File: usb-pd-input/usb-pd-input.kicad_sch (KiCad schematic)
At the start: 2 parts, among them J1 USB_C_Receptacle, U1 CH224K

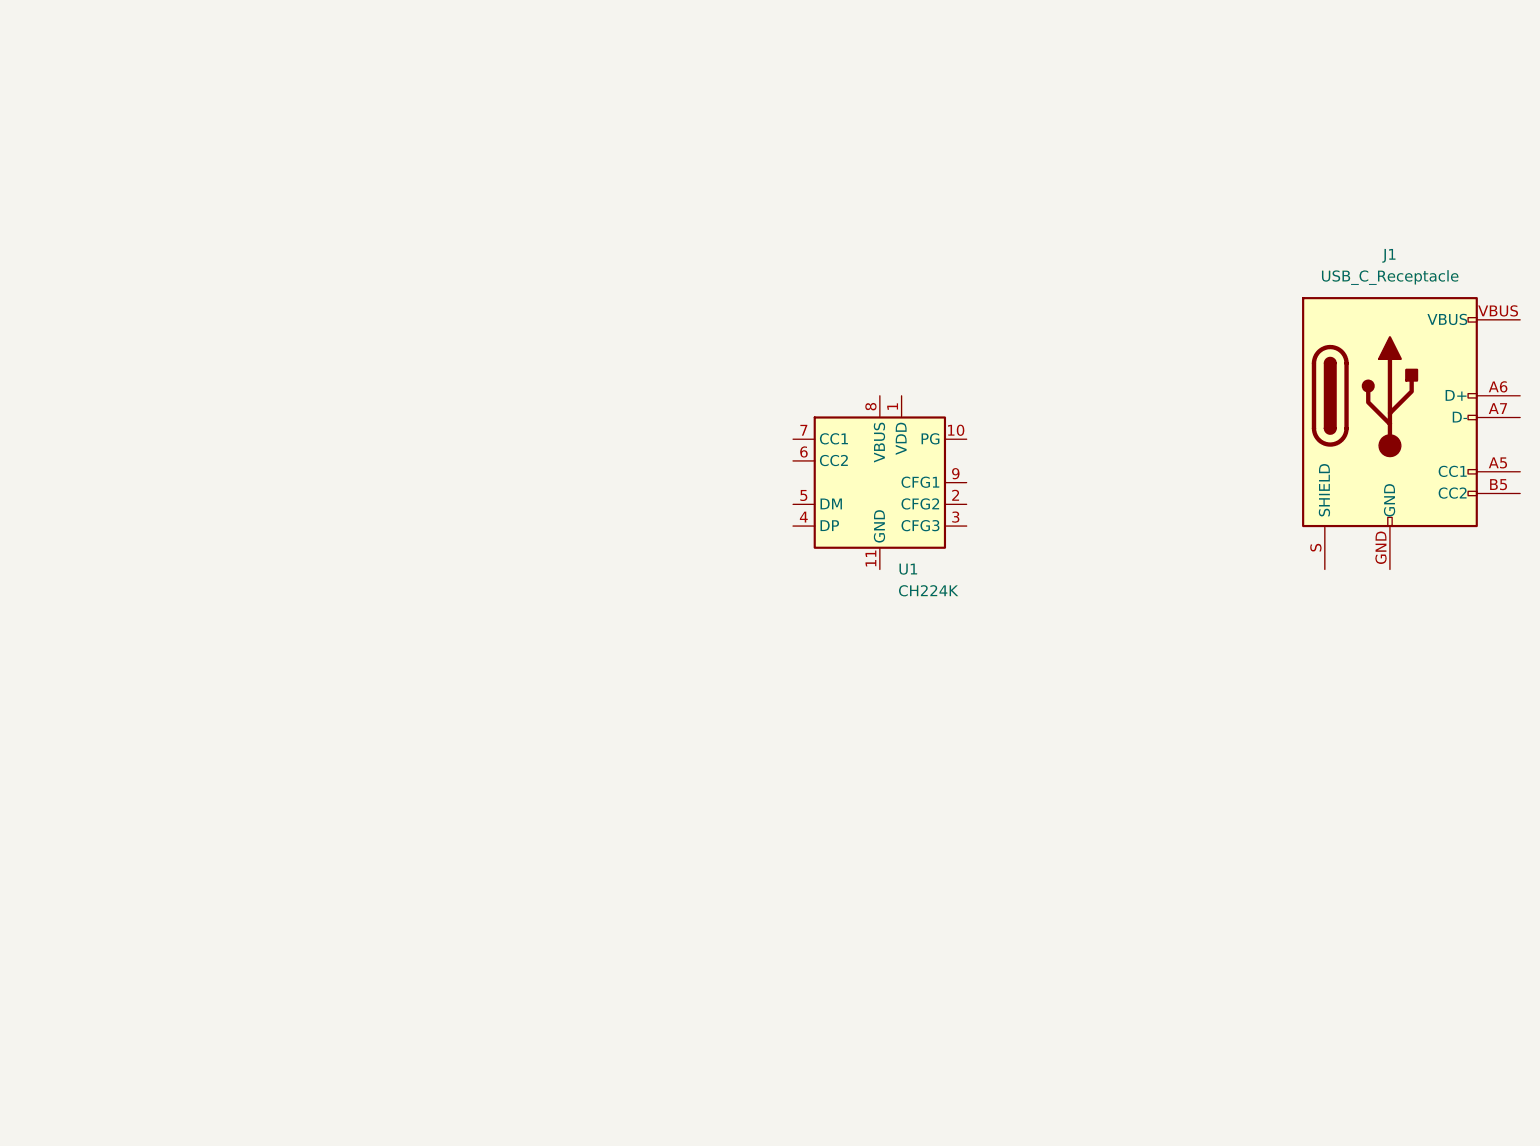
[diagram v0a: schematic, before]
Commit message: Added USB-PD rough-in
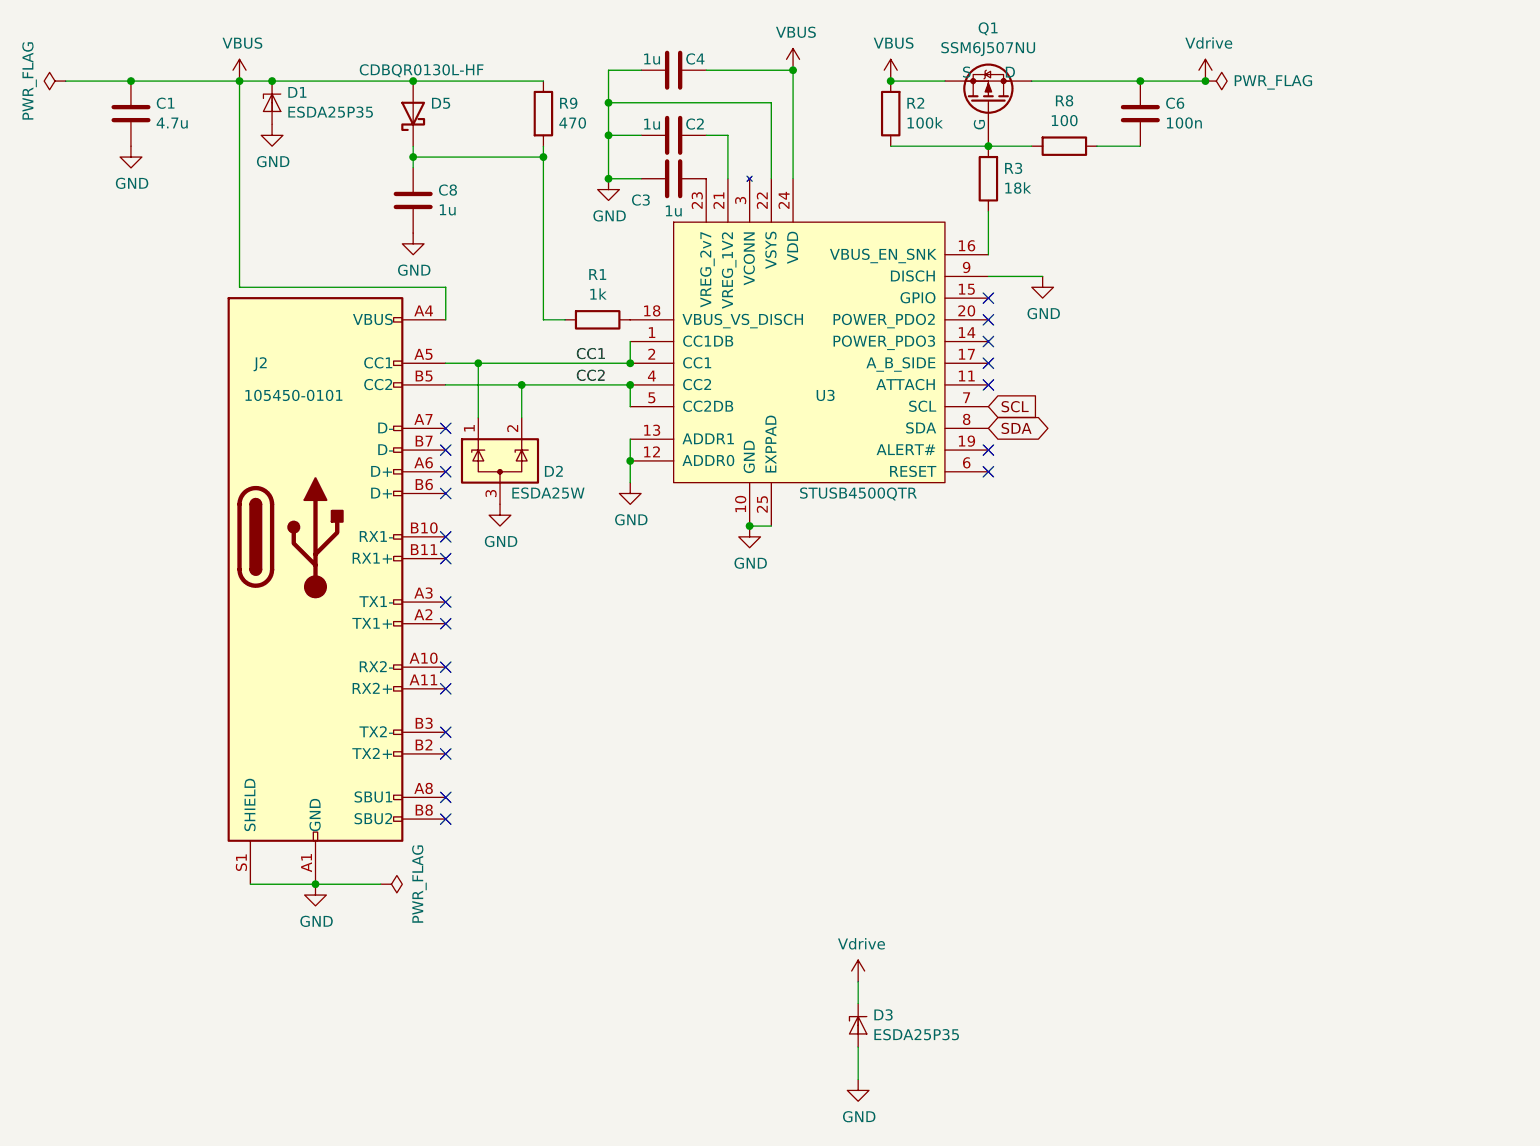
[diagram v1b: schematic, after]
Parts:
- removed J1: USB_C_Receptacle, PCM_SparkFun-Connector:USB-C_16, symbol PCM_SparkFun-Connector:USB_C_Receptacle
- removed U1: CH224K, Package_SO:SSOP-10-1EP_3.9x4.9mm_P1mm_EP2.1x3.3mm, symbol Interface_USB:CH224K
- added C1: 4.7u, Capacitor_SMD:C_0603_1608Metric, symbol Device:C
- added C2, C3, C4: 1u, Capacitor_SMD:C_0603_1608Metric, symbol Device:C
- added C6: 100n, Capacitor_SMD:C_0402_1005Metric, symbol Device:C
- added C8: 1u, Capacitor_SMD:C_0402_1005Metric, symbol Device:C
- added D1, D3: ESDA25P35, rhinocerose-diodes:ESDA25P351U1M, symbol symbol:ESDA25P35
- added D2: ESDA25W, Package_TO_SOT_SMD:SOT-323_SC-70, symbol symbol:ESDA25W
- added D5: D_Schottky, Diode_SMD:D_0402_1005Metric, symbol Device:D_Schottky
- added J2: 105450-0101, fpx:MOLEX_105450-0101, symbol fpx-rescue:USB_C_Receptacle-Connector
- added Q1: SSM6J507NU, rhinocerose-transistors:SSM6J507NULF, symbol symbol:SSM6J507NU
- added R1: 1k, Resistor_SMD:R_0402_1005Metric, symbol Device:R
- added R2: 100k, Resistor_SMD:R_0402_1005Metric, symbol Device:R
- added R3: 18k, Resistor_SMD:R_0402_1005Metric, symbol Device:R
- added R8: 100, Resistor_SMD:R_0402_1005Metric, symbol Device:R
- added R9: 470, Resistor_SMD:R_0402_1005Metric, symbol Device:R
- added U3: STUSB4500, Package_DFN_QFN:QFN-24-1EP_4x4mm_P0.5mm_EP2.7x2.6mm, symbol symbol:STUSB4500
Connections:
- new net: Q1.3 (G), R2.1, R3.2, R8.2
- new net: C3.1, U3.23 (VREG_2v7)
- new net: C2.1, U3.21 (VREG_1V2)
- new net: R1.1, U3.18 (VBUS_VS_DISCH)
- new net: C8.1, D5.1 (K), R1.2, R9.2
- new net: R3.1, U3.16 (VBUS_EN_SNK)
- new net: C6.2, R8.1
- new net CC1: D2.1 (K), J2.A5 (CC1), U3.1 (CC1DB), U3.2 (CC1)
- new net CC2: D2.2 (K), J2.B5 (CC2), U3.4 (CC2), U3.5 (CC2DB)
- new net GND: C1.2, C2.2, C3.2, C4.2, C8.2, D1.2 (A), D2.3 (A), D3.2 (A), J2.A1 (GND), J2.A12 (GND), J2.B1 (GND), J2.B12 (GND), J2.S1 (SHIELD), U3.10 (GND), U3.12 (ADDR0), U3.13 (ADDR1), U3.22 (VSYS), U3.25 (EXPPAD), U3.9 (DISCH)
- new net SCL: U3.7 (SCL)
- new net SDA: U3.8 (SDA)
- new net VBUS: C1.1, C4.1, D1.1 (K1), D5.2 (A), J2.A4 (VBUS), J2.A9 (VBUS), J2.B4 (VBUS), J2.B9 (VBUS), Q1.4 (S), Q1.S, R2.2, R9.1, U3.24 (VDD)
- new net Vdrive: C6.1, D3.1 (K1), Q1.1 (D), Q1.2 (D), Q1.5 (D), Q1.6 (D), Q1.D
- no-connect marks 0 -> 21

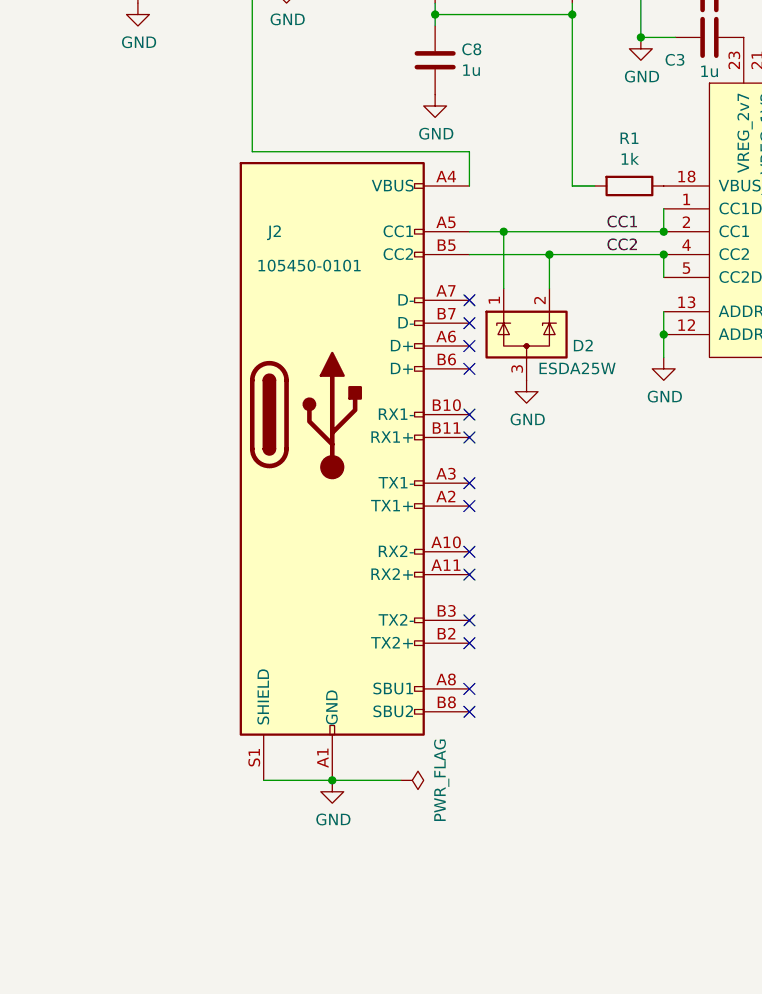
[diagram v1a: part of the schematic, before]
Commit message: Added CH224 schematic
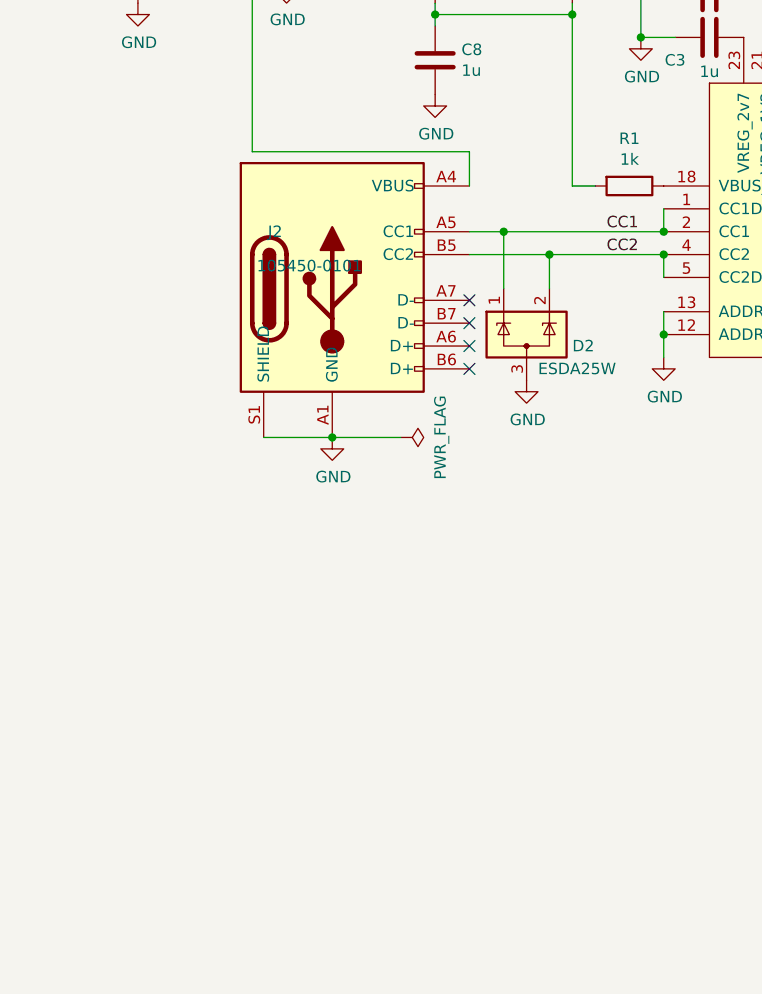
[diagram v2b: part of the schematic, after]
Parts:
- J2: footprint fpx:MOLEX_105450-0101 -> rhinocerose-jacks:CUI_UJ20-C-V-C-2-SMT-TR; symbol fpx-rescue:USB_C_Receptacle-Connector -> rhinocerose-connectors:UJ20-C-V-C-2-SMT-TR; CREATOR (none) -> KARTHIK; MANUFACTURER (none) -> Same Sky; MAXIMUM_PACKAGE_HEIGHT (none) -> 10.75 mm; PARTREV (none) -> 1.02; STANDARD (none) -> Manufacturer Recommendation
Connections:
- no-connect marks 21 -> 11
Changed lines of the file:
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@@
 	)
 	(junction
-		(at 57.15 127)
+		(at 57.15 88.9)
 		(diameter 0)
 		(color 0 0 0 0)
@@
 	)
 	(no_connect
-		(at 72.39 93.98)
-	)
-	(no_connect
 		(at 72.39 78.74)
 	)
 	(no_connect
-		(at 72.39 111.76)
-	)
-	(no_connect
-		(at 72.39 109.22)
-	)
-	(no_connect
-		(at 72.39 104.14)
-	)
-	(no_connect
 		(at 72.39 73.66)
 	)
@@
 	)
 	(no_connect
-		(at 72.39 96.52)
-	)
-	(no_connect
-		(at 72.39 119.38)
-	)
-	(no_connect
 		(at 135.89 78.74)
 	)
@@
 	)
 	(no_connect
-		(at 72.39 88.9)
-	)
-	(no_connect
-		(at 72.39 116.84)
-	)
-	(no_connect
 		(at 135.89 66.04)
 	)
@@
 		(at 135.89 63.5)
 	)
-	(no_connect
-		(at 72.39 86.36)
-	)
-	(no_connect
-		(at 72.39 101.6)
-	)
 	(wire
 		(pts
@@
 	(wire
 		(pts
-			(xy 49.53 127) (xy 57.15 127)
+			(xy 49.53 88.9) (xy 57.15 88.9)
 		)
 		(stroke
@@
 	(wire
 		(pts
-			(xy 57.15 127) (xy 64.77 127)
+			(xy 57.15 88.9) (xy 64.77 88.9)
 		)
 		(stroke
@@
 	(symbol
 		(lib_id "power:GND")
-		(at 57.15 127 0)
+		(at 57.15 88.9 0)
 		(unit 1)
 		(exclude_from_sim no)
@@
 		(dnp no)
 		(property "Reference" "#PWR01"
-			(at 57.15 133.35 0)
+			(at 57.15 95.25 0)
 			(effects
 				(font
@@
 		)
 		(property "Value" "GND"
-			(at 57.277 131.3942 0)
+			(at 57.277 93.2942 0)
 			(effects
 				(font
@@
 		)
 		(property "Footprint" ""
-			(at 57.15 127 0)
+			(at 57.15 88.9 0)
 			(effects
 				(font
@@
 		)
 		(property "Datasheet" ""
-			(at 57.15 127 0)
+			(at 57.15 88.9 0)
 			(effects
 				(font
@@
 		)
 		(property "Description" ""
-			(at 57.15 127 0)
+			(at 57.15 88.9 0)
 			(effects
 				(font
@@
 	(symbol
 		(lib_id "power:PWR_FLAG")
-		(at 64.77 127 270)
+		(at 64.77 88.9 270)
 		(unit 1)
 		(exclude_from_sim no)
@@
 		(dnp no)
 		(property "Reference" "#FLG01"
-			(at 66.675 127 0)
+			(at 66.675 88.9 0)
 			(effects
 				(font
@@
 		)
 		(property "Value" "PWR_FLAG"
-			(at 69.1642 127 0)
+			(at 69.1642 88.9 0)
 			(effects
 				(font
@@
 		)
 		(property "Footprint" ""
-			(at 64.77 127 0)
+			(at 64.77 88.9 0)
 			(effects
 				(font
@@
 		)
 		(property "Datasheet" "~"
-			(at 64.77 127 0)
+			(at 64.77 88.9 0)
 			(effects
 				(font
@@
 		)
 		(property "Description" ""
-			(at 64.77 127 0)
+			(at 64.77 88.9 0)
 			(effects
 				(font
@@
 	)
 	(symbol
-		(lib_id "fpx-rescue:USB_C_Receptacle-Connector")
+		(lib_id "rhinocerose-connectors:UJ20-C-V-C-2-SMT-TR")
 		(at 57.15 86.36 0)
 		(unit 1)
@@
 			)
 		)
-		(property "Footprint" "fpx:MOLEX_105450-0101"
-			(at 60.96 86.36 0)
+		(property "Footprint" "rhinocerose-jacks:CUI_UJ20-C-V-C-2-SMT-TR"
+			(at 57.15 86.36 0)
 			(effects
 				(font
 					(size 1.27 1.27)
 				)
+				(justify bottom)
 				(hide yes)
 			)
 		)
 		(property "Datasheet" "https://www.usb.org/sites/default/files/documents/usb_type-c.zip"
-			(at 60.96 86.36 0)
+			(at 57.15 86.36 0)
 			(effects
 				(font
@@
 					(size 1.27 1.27)
 				)
+				(hide yes)
 			)
 		)
@@
 			)
 		)
+		(property "PARTREV" "1.02"
+			(at 57.15 86.36 0)
+			(effects
+				(font
+					(size 1.27 1.27)
+				)
+				(justify bottom)
+				(hide yes)
+			)
+		)
+		(property "MANUFACTURER" "Same Sky"
+			(at 57.15 86.36 0)
+			(effects
+				(font
+					(size 1.27 1.27)
+				)
+				(justify bottom)
+				(hide yes)
+			)
+		)
+		(property "CREATOR" "KARTHIK"
+			(at 57.15 86.36 0)
+			(effects
+				(font
+					(size 1.27 1.27)
+				)
+				(justify bottom)
+				(hide yes)
+			)
+		)
+		(property "MAXIMUM_PACKAGE_HEIGHT" "10.75 mm"
+			(at 57.15 86.36 0)
+			(effects
+				(font
+					(size 1.27 1.27)
+				)
+				(justify bottom)
+				(hide yes)
+			)
+		)
+		(property "STANDARD" "Manufacturer Recommendation"
+			(at 57.15 86.36 0)
+			(effects
+				(font
+					(size 1.27 1.27)
+				)
+				(justify bottom)
+				(hide yes)
+			)
+		)
 		(pin "A4"
 		)
@@
 		(pin "B12"
 		)
-		(pin "A11"
-		)
 		(pin "A9"
 		)
-		(pin "B11"
-		)
 		(pin "B7"
 		)
-		(pin "A2"
-		)
 		(pin "B6"
 		)
-		(pin "A10"
-		)
 		(pin "B5"
 		)
-		(pin "B10"
-		)
-		(pin "A3"
-		)
 		(pin "A7"
 		)
-		(pin "B8"
-		)
-		(pin "B3"
-		)
 		(pin "A5"
 		)
 		(pin "B9"
 		)
-		(pin "A8"
-		)
 		(pin "B4"
 		)
 		(pin "A6"
 		)
-		(pin "B2"
-		)
 		(instances
